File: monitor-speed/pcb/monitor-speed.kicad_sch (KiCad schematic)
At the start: 1 part

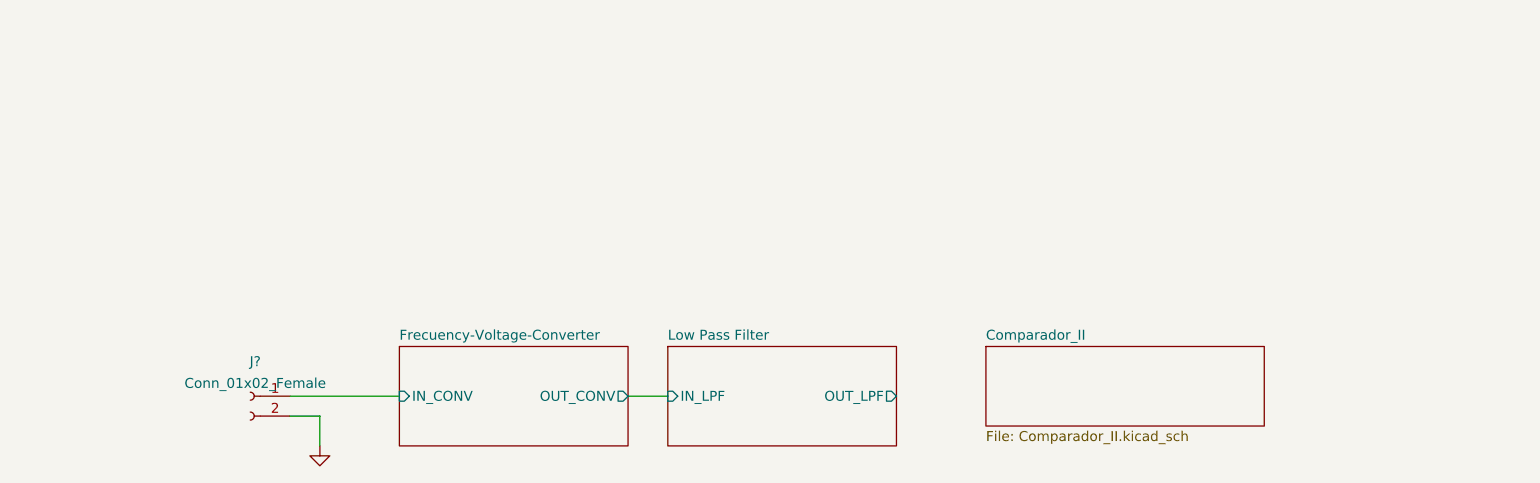
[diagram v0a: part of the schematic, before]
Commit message: Monitor-Speed: New Schematic
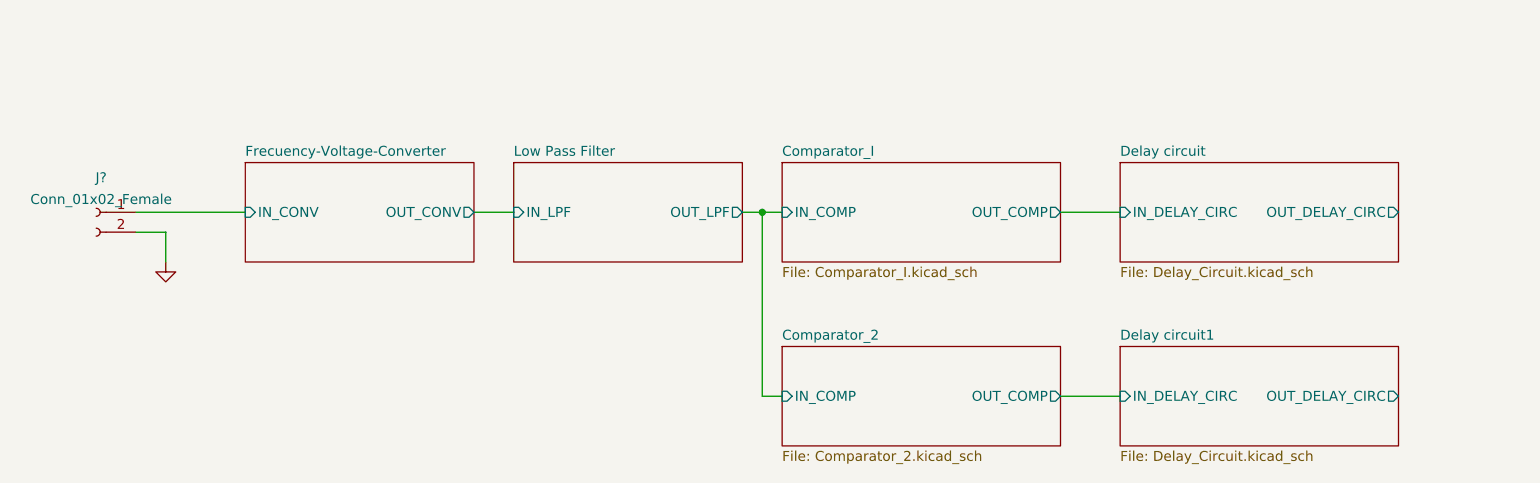
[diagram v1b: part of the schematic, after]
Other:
- sheet Comparador_II renamed Comparator_I
- added sheet Comparator_2 (Comparator_2.kicad_sch)
- added sheet Delay circuit (Delay_Circuit.kicad_sch)
- added sheet Delay circuit1 (Delay_Circuit.kicad_sch)
- sheet Comparator_I: file Comparador_II.kicad_sch -> Comparator_I.kicad_sch
- sheet Comparator_I ports: added IN_COMP, OUT_COMP; removed none
- moved on the sheet: J?

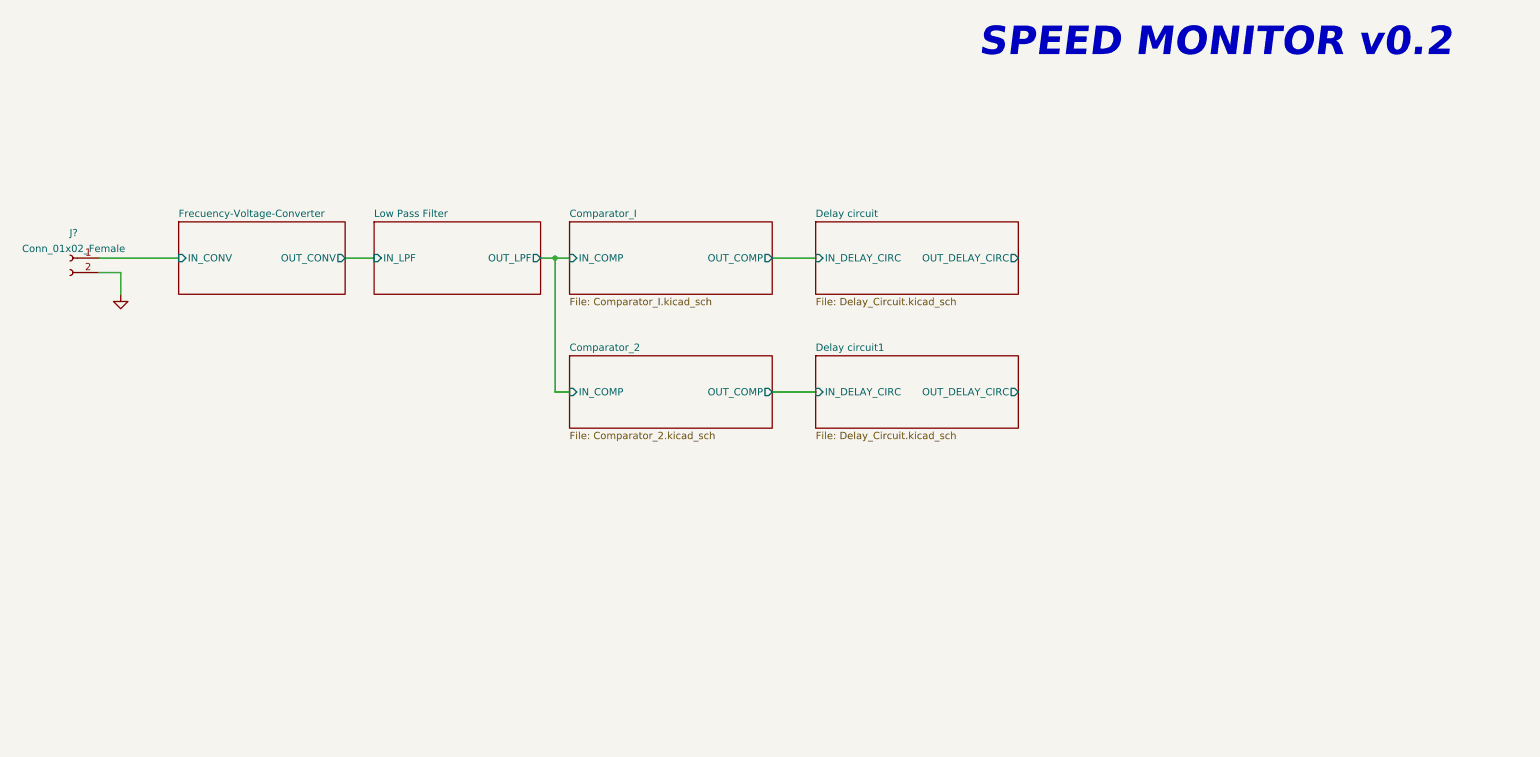
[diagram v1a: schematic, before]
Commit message: Monitor-Speed: Add Relay Circuit
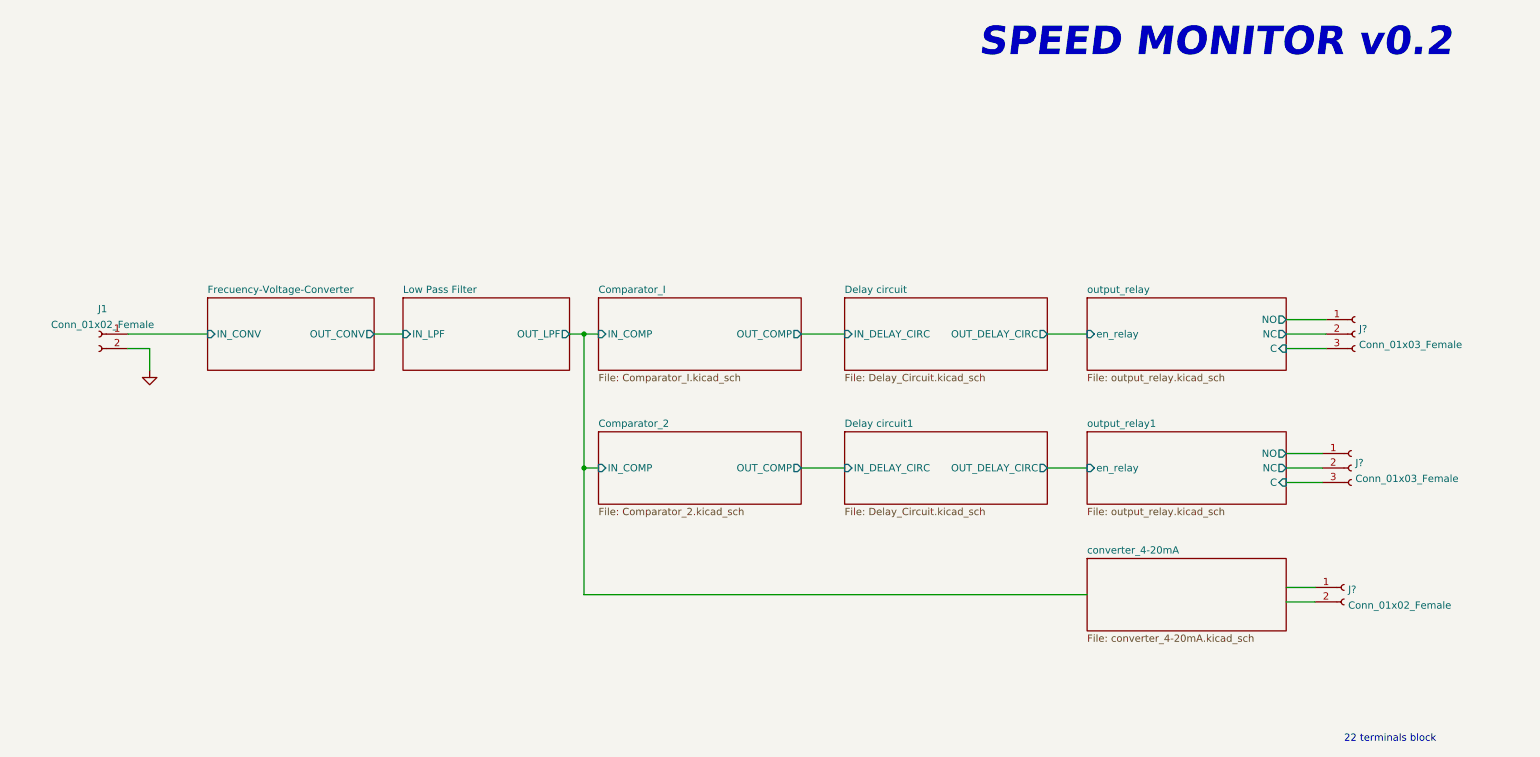
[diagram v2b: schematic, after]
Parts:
- added J? (x2): Conn_01x03_Female, eec:TE-282841-3-0, symbol Connector:Conn_01x03_Female
- added J?: Conn_01x02_Female, symbol Connector:Conn_01x02_Female
- gave numbers to parts that had none: 1
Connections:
- new net output_relay/C: J?.3 (Pin_3)
- new net output_relay/NC: J?.2 (Pin_2)
- new net output_relay/NO: J?.1 (Pin_1)
- new net output_relay1/C: J?.3 (Pin_3)
- new net output_relay1/NC: J?.2 (Pin_2)
- new net output_relay1/NO: J?.1 (Pin_1)
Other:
- added sheet converter_4-20mA (converter_4-20mA.kicad_sch)
- added sheet output_relay (output_relay.kicad_sch)
- added sheet output_relay1 (output_relay.kicad_sch)
- note added: "22 terminals block"
- company: (none) -> Universidad Tecnologica Nacional
- title: (none) -> Monitor speed 
- moved on the sheet: J1

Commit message: Agregue capas interiores....
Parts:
- gave numbers to parts that had none: 3
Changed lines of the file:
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@@
   (symbol (lib_id "Connector:Conn_01x03_Female") (at 254.635 102.235 0) (unit 1)
     (in_bom yes) (on_board yes) (fields_autoplaced)
-    (property "Reference" "J?" (id 0) (at 255.3462 101.3265 0)
+    (property "Reference" "J3" (id 0) (at 255.3462 101.3265 0)
       (effects (font (size 1.27 1.27)) (justify left))
     )
@@
   (symbol (lib_id "Connector:Conn_01x02_Female") (at 253.365 123.19 0) (unit 1)
     (in_bom yes) (on_board yes) (fields_autoplaced)
-    (property "Reference" "J?" (id 0) (at 254.0762 123.5515 0)
+    (property "Reference" "J2" (id 0) (at 254.0762 123.5515 0)
       (effects (font (size 1.27 1.27)) (justify left))
     )
@@
   (symbol (lib_id "Connector:Conn_01x03_Female") (at 255.27 78.74 0) (unit 1)
     (in_bom yes) (on_board yes) (fields_autoplaced)
-    (property "Reference" "J?" (id 0) (at 255.9812 77.8315 0)
+    (property "Reference" "J4" (id 0) (at 255.9812 77.8315 0)
       (effects (font (size 1.27 1.27)) (justify left))
     )
@@
       (reference "#PWR039") (unit 1) (value "GND") (footprint "")
     )
+    (path "/f47e5bea-e25b-470c-b755-473b68193ada/32553301-461e-4184-8975-7f2f74daa1e8"
+      (reference "#PWR0101") (unit 1) (value "+12") (footprint "")
+    )
     (path "/01106a52-6b7d-40fd-b165-c927be1f6a1d/00000000-0000-0000-0000-00006131287a"
       (reference "#PWR0110") (unit 1) (value "GND") (footprint "")
@@
       (reference "#PWR0123") (unit 1) (value "GND") (footprint "")
     )
-    (path "/f47e5bea-e25b-470c-b755-473b68193ada/32553301-461e-4184-8975-7f2f74daa1e8"
-      (reference "#PWR?") (unit 1) (value "+12") (footprint "")
-    )
     (path "/01106a52-6b7d-40fd-b165-c927be1f6a1d/c24d8954-27a8-4850-9e38-ffdbeb71bd91"
       (reference "C1") (unit 1) (value "100nF") (footprint "Capacitor_SMD:C_0603_1608Metric_Pad1.08x0.95mm_HandSolder")
@@
       (reference "J1") (unit 1) (value "Conn_01x02_Female") (footprint "")
     )
+    (path "/25d3f6fc-1324-40cb-a95f-24af8107b6ca"
+      (reference "J2") (unit 1) (value "Conn_01x02_Female") (footprint "")
+    )
     (path "/0cd0aafc-b20f-4c18-b692-78a357cba885"
-      (reference "J?") (unit 1) (value "Conn_01x03_Female") (footprint "eec:TE-282841-3-0")
-    )
-    (path "/25d3f6fc-1324-40cb-a95f-24af8107b6ca"
-      (reference "J?") (unit 1) (value "Conn_01x02_Female") (footprint "")
+      (reference "J3") (unit 1) (value "Conn_01x03_Female") (footprint "eec:TE-282841-3-0")
     )
     (path "/820c4e56-54a6-4bbd-8f19-ee87ad8a593c"
-      (reference "J?") (unit 1) (value "Conn_01x03_Female") (footprint "eec:TE-282841-3-0")
+      (reference "J4") (unit 1) (value "Conn_01x03_Female") (footprint "eec:TE-282841-3-0")
     )
     (path "/9ab52dfd-8d71-4050-bfe4-ebd78ae16dff/00000000-0000-0000-0000-000061350345"
